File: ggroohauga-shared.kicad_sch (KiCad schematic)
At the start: 11 parts

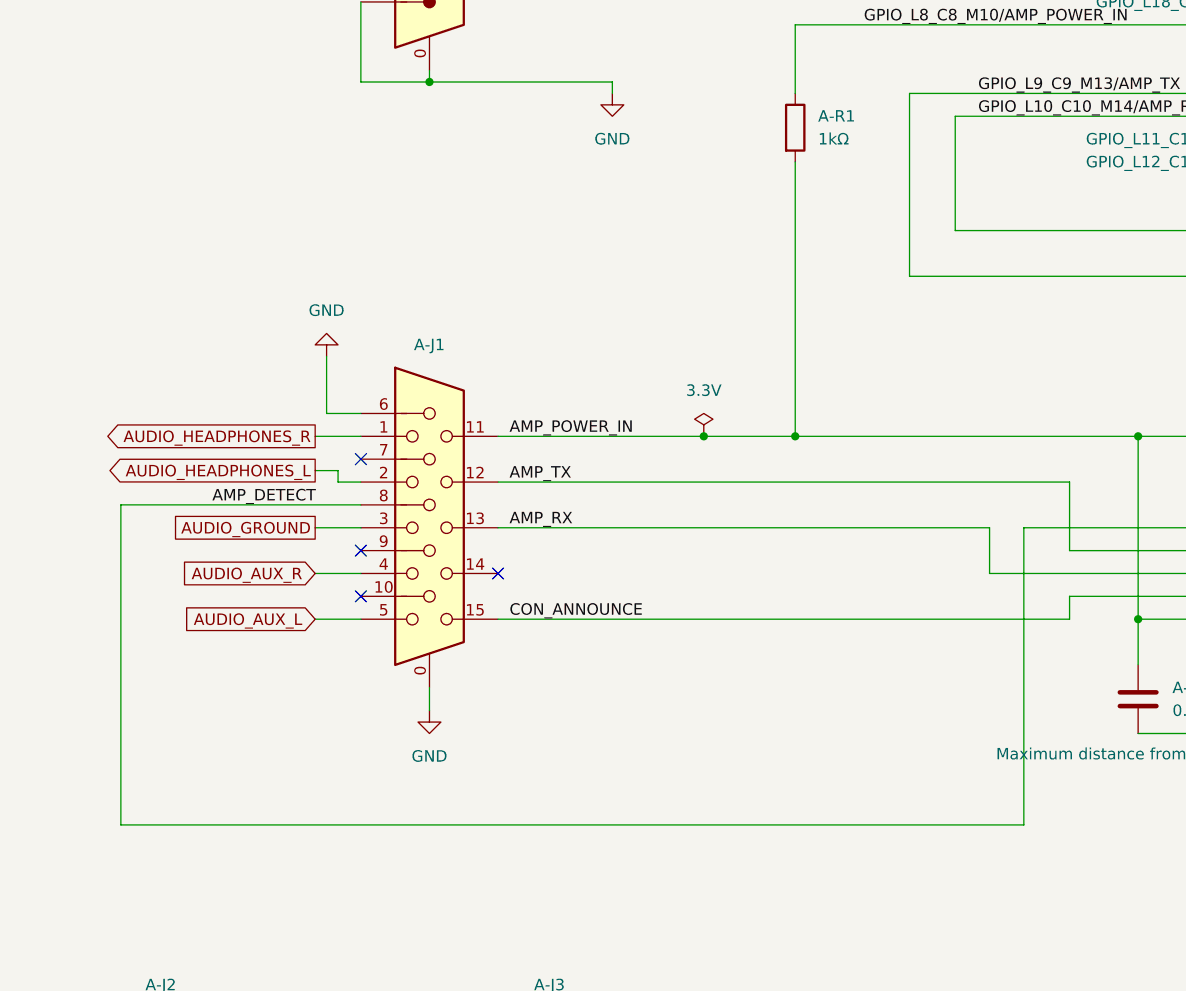
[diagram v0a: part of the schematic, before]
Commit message: Add pull-up resistors to amplifier detect and RX inputs
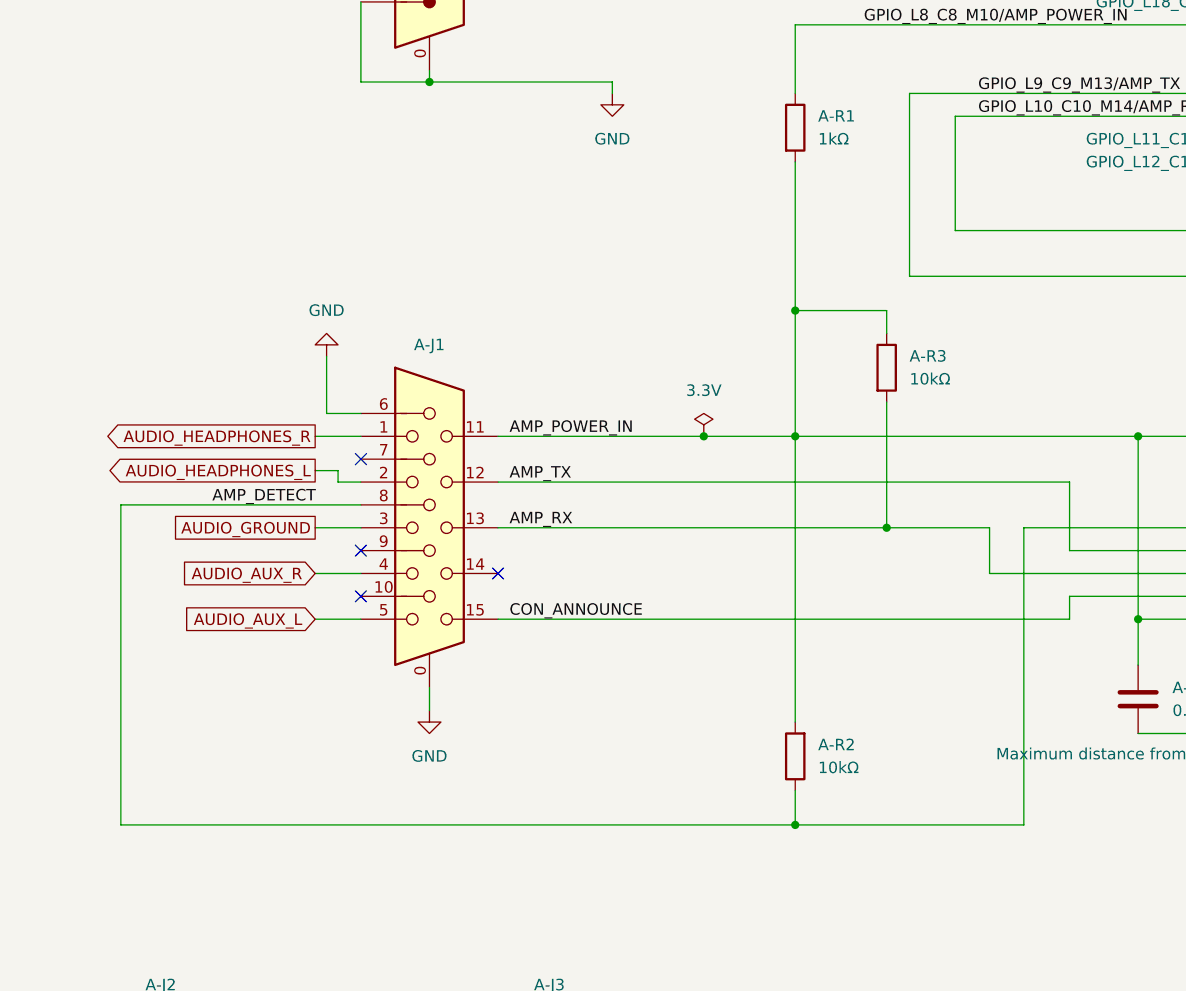
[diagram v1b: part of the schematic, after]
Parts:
- added A-R2, A-R3: 10kΩ, Resistor_SMD:R_0805_2012Metric_Pad1.20x1.40mm_HandSolder, symbol Device:R
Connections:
- net AMP_DETECT: now also A-R2.1
- net AMP_POWER_IN: now also A-R2.2, A-R3.1
- net AMP_RX: now also A-R3.2
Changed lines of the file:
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@@
 	)
 	(junction
+		(at 114.3 121.92)
+		(diameter 0)
+		(color 0 0 0 0)
+	)
+	(junction
+		(at 104.14 154.94)
+		(diameter 0)
+		(color 0 0 0 0)
+	)
+	(junction
 		(at 104.14 111.76)
 		(diameter 0)
@@
 		(color 0 0 0 0)
 	)
+	(junction
+		(at 104.14 97.79)
+		(diameter 0)
+		(color 0 0 0 0)
+	)
 	(no_connect
 		(at 55.88 58.42)
@@
 	(wire
 		(pts
+			(xy 104.14 111.76) (xy 104.14 143.51)
+		)
+		(stroke
+			(width 0)
+			(type default)
+		)
+	)
+	(wire
+		(pts
 			(xy 154.94 38.1) (xy 162.56 38.1)
 		)
@@
 	(wire
 		(pts
-			(xy 160.02 81.28) (xy 162.56 81.28)
+			(xy 104.14 154.94) (xy 129.54 154.94)
 		)
 		(stroke
@@
 	(wire
 		(pts
-			(xy 109.22 60.96) (xy 162.56 60.96)
+			(xy 160.02 81.28) (xy 162.56 81.28)
 		)
 		(stroke
@@
 	(wire
 		(pts
-			(xy 71.12 40.64) (xy 109.22 40.64)
+			(xy 109.22 60.96) (xy 162.56 60.96)
 		)
 		(stroke
@@
 	(wire
 		(pts
-			(xy 63.5 72.39) (xy 83.82 72.39)
+			(xy 71.12 40.64) (xy 109.22 40.64)
 		)
 		(stroke
@@
 	(wire
 		(pts
-			(xy 71.12 111.76) (xy 93.98 111.76)
+			(xy 63.5 72.39) (xy 83.82 72.39)
 		)
 		(stroke
@@
 	(wire
 		(pts
-			(xy 29.21 154.94) (xy 129.54 154.94)
+			(xy 71.12 111.76) (xy 93.98 111.76)
 		)
 		(stroke
@@
 	(wire
 		(pts
-			(xy 104.14 81.28) (xy 104.14 111.76)
+			(xy 104.14 81.28) (xy 104.14 97.79)
+		)
+		(stroke
+			(width 0)
+			(type default)
+		)
+	)
+	(wire
+		(pts
+			(xy 114.3 121.92) (xy 125.73 121.92)
 		)
 		(stroke
@@
 	(wire
 		(pts
+			(xy 104.14 151.13) (xy 104.14 154.94)
+		)
+		(stroke
+			(width 0)
+			(type default)
+		)
+	)
+	(wire
+		(pts
 			(xy 83.82 72.39) (xy 83.82 73.66)
 		)
@@
 	(wire
 		(pts
-			(xy 71.12 121.92) (xy 125.73 121.92)
+			(xy 71.12 121.92) (xy 114.3 121.92)
 		)
 		(stroke
@@
 	(wire
 		(pts
+			(xy 104.14 97.79) (xy 114.3 97.79)
+		)
+		(stroke
+			(width 0)
+			(type default)
+		)
+	)
+	(wire
+		(pts
 			(xy 40.64 181.61) (xy 45.72 181.61)
 		)
@@
 	(wire
 		(pts
+			(xy 104.14 97.79) (xy 104.14 111.76)
+		)
+		(stroke
+			(width 0)
+			(type default)
+		)
+	)
+	(wire
+		(pts
 			(xy 245.11 68.58) (xy 245.11 129.54)
 		)
@@
 	(wire
 		(pts
+			(xy 114.3 97.79) (xy 114.3 100.33)
+		)
+		(stroke
+			(width 0)
+			(type default)
+		)
+	)
+	(wire
+		(pts
 			(xy 50.8 55.88) (xy 55.88 55.88)
 		)
@@
 	(wire
 		(pts
+			(xy 114.3 107.95) (xy 114.3 121.92)
+		)
+		(stroke
+			(width 0)
+			(type default)
+		)
+	)
+	(wire
+		(pts
 			(xy 129.54 121.92) (xy 129.54 154.94)
 		)
@@
 	(wire
 		(pts
+			(xy 29.21 154.94) (xy 104.14 154.94)
+		)
+		(stroke
+			(width 0)
+			(type default)
+		)
+	)
+	(wire
+		(pts
 			(xy 171.45 142.24) (xy 171.45 144.78)
 		)
@@
 	)
 	(symbol
+		(lib_id "Device:R")
+		(at 114.3 104.14 0)
+		(unit 1)
+		(exclude_from_sim no)
+		(in_bom yes)
+		(on_board yes)
+		(dnp no)
+		(fields_autoplaced yes)
+		(property "Reference" "A-R3"
+			(at 116.84 102.8699 0)
+			(effects
+				(font
+					(size 1.27 1.27)
+				)
+				(justify left)
+			)
+		)
+		(property "Value" "10kΩ"
+			(at 116.84 105.4099 0)
+			(effects
+				(font
+					(size 1.27 1.27)
+				)
+				(justify left)
+			)
+		)
+		(property "Footprint" "Resistor_SMD:R_0805_2012Metric_Pad1.20x1.40mm_HandSolder"
+			(at 112.522 104.14 90)
+			(effects
+				(font
+					(size 1.27 1.27)
+				)
+				(hide yes)
+			)
+		)
+		(property "Datasheet" "~"
+			(at 114.3 104.14 0)
+			(effects
+				(font
+					(size 1.27 1.27)
+				)
+				(hide yes)
+			)
+		)
+		(property "Description" "Resistor"
+			(at 114.3 104.14 0)
+			(effects
+				(font
+					(size 1.27 1.27)
+				)
+				(hide yes)
+			)
+		)
+		(pin "1"
+		)
+		(pin "2"
+		)
+		(instances
+			(project ""
+				(path "/40d11306-2494-4bd8-b540-c25b2be9aaac/d8f68aac-e4b3-42cf-adb2-95c1a8c35ecf"
+					(reference "A-R3")
+					(unit 1)
+				)
+			)
+		)
+	)
+	(symbol
 		(lib_id "Connector_Audio:AudioJack3")
 		(at 35.56 181.61 0)
@@
 					(unit 1)
 				)
+			)
+		)
+	)
+	(symbol
+		(lib_id "Device:R")
+		(at 104.14 147.32 180)
+		(unit 1)
+		(exclude_from_sim no)
+		(in_bom yes)
+		(on_board yes)
+		(dnp no)
+		(fields_autoplaced yes)
+		(property "Reference" "A-R2"
+			(at 106.68 146.0499 0)
+			(effects
+				(font
+					(size 1.27 1.27)
+				)
+				(justify right)
+			)
+		)
+		(property "Value" "10kΩ"
+			(at 106.68 148.5899 0)
+			(effects
+				(font
+					(size 1.27 1.27)
+				)
+				(justify right)
+			)
+		)
+		(property "Footprint" "Resistor_SMD:R_0805_2012Metric_Pad1.20x1.40mm_HandSolder"
+			(at 105.918 147.32 90)
+			(effects
+				(font
+					(size 1.27 1.27)
+				)
+				(hide yes)
+			)
+		)
+		(property "Datasheet" "~"
+			(at 104.14 147.32 0)
+			(effects
+				(font
+					(size 1.27 1.27)
+				)
+				(hide yes)
+			)
+		)
+		(property "Description" "Resistor"
+			(at 104.14 147.32 0)
+			(effects
+				(font
+					(size 1.27 1.27)
+				)
+				(hide yes)
+			)
+		)
+		(pin "1"
+		)
+		(pin "2"
+		)
+		(instances
+			(project ""
+				(path "/40d11306-2494-4bd8-b540-c25b2be9aaac/d8f68aac-e4b3-42cf-adb2-95c1a8c35ecf"
+					(reference "A-R2")
+					(unit 1)
+				)
